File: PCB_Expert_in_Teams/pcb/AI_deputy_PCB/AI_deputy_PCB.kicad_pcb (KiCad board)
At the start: 2 copper layers, 15 parts, among them IC1 DA7280-00FVC, J1 Piezo Electric, U1 ESP32-WROOM-32UE_M113EH6400UH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, Y2 ABM8-40.000MHz-10-D1G-T

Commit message: progress on PCB + matlab calculations
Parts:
- removed U1: ESP32-WROOM-32UE_M113EH6400UH3Q0_, EXT_AI_DEPUTY_Library:MODULE_ESP32-WROOM-32UE_M113EH6400UH3Q0_
- removed Y2: ABM8-40.000MHz-10-D1G-T, EXT_AI_DEPUTY_Library:ABM810000MHZ12D2W
- added C10: 1u, Capacitor_SMD:C_0805_2012Metric_Pad1.18x1.45mm_HandSolder, F.Cu at (71.2, 62.7)
- added C11: 100n, Capacitor_SMD:C_0805_2012Metric_Pad1.18x1.45mm_HandSolder, F.Cu at (76.1, 53.6)
- added C12: 1u, Capacitor_SMD:C_0805_2012Metric_Pad1.18x1.45mm_HandSolder, F.Cu at (76.1, 56.6)
- added C13: 100n, Capacitor_SMD:C_0805_2012Metric_Pad1.18x1.45mm_HandSolder, F.Cu at (76.1, 59.6)
- added C14: 1u, Capacitor_SMD:C_0805_2012Metric_Pad1.18x1.45mm_HandSolder, F.Cu at (76.1, 62.7)
- added C15: 10u, Capacitor_SMD:C_0805_2012Metric_Pad1.18x1.45mm_HandSolder, F.Cu at (80.9, 53.6)
- added C16: 100n, Capacitor_SMD:C_0805_2012Metric_Pad1.18x1.45mm_HandSolder, F.Cu at (80.9, 56.6)
- added C17: 10u, Capacitor_SMD:C_0805_2012Metric_Pad1.18x1.45mm_HandSolder, F.Cu at (80.9, 59.6)
- added C18: 100n, Capacitor_SMD:C_0805_2012Metric_Pad1.18x1.45mm_HandSolder, F.Cu at (80.9, 62.7)
- added C19: 0.1u, Capacitor_SMD:C_0805_2012Metric_Pad1.18x1.45mm_HandSolder, F.Cu at (100.2, 71.5)
- added C20: 0.1u, Capacitor_SMD:C_0805_2012Metric_Pad1.18x1.45mm_HandSolder, F.Cu at (100.2, 74.5)
- added C21: 0.1u, Capacitor_SMD:C_0805_2012Metric_Pad1.18x1.45mm_HandSolder, F.Cu at (100.2, 77.5)
- added C22: 0.1u, Capacitor_SMD:C_0805_2012Metric_Pad1.18x1.45mm_HandSolder, F.Cu at (100.2, 80.6)
- added C23: 0.1u, Capacitor_SMD:C_0805_2012Metric_Pad1.18x1.45mm_HandSolder, F.Cu at (100.2, 83.6)
- added C24: 1u, Capacitor_SMD:C_0805_2012Metric_Pad1.18x1.45mm_HandSolder, F.Cu at (100.2, 86.6)
- added C25: 0.1u, Capacitor_SMD:C_0805_2012Metric_Pad1.18x1.45mm_HandSolder, F.Cu at (100.2, 89.6)
- added C26: 1u, Capacitor_SMD:C_0805_2012Metric_Pad1.18x1.45mm_HandSolder, F.Cu at (100.2, 92.6)
- added D1: LED, LED_SMD:LED_0805_2012Metric_Pad1.15x1.40mm_HandSolder, F.Cu at (86.5, 89.6)
- added IC2: DA7281-00FVC, EXT_AI_DEPUTY_Library:QFN65P300X300X84-12N, F.Cu at (66.2, 60.1)
- added IC3: DA7282-00FVC, EXT_AI_DEPUTY_Library:QFN65P300X300X84-12N, F.Cu at (66.2, 65.4)
- added IC4: IS31AP2005-SLS2-TR, EXT_AI_DEPUTY_Library:SOP65P490X110-8N, F.Cu at (131.3, 84.9)
- added IC5: IS31AP2005-SLS2-TR, EXT_AI_DEPUTY_Library:SOP65P490X110-8N, F.Cu at (131.3, 89.5)
- added IC6: LM25576QMH_NOPB, EXT_AI_DEPUTY_Library:SOP65P640X110-21N, F.Cu at (172.1, 74.1)
- added J10: OUTPUT Haptic B (Neck R), Connector_JST:JST_XH_S2B-XH-A_1x02_P2.50mm_Horizontal, F.Cu at (76.4, 41.9)
- added J11: OUTPUT Haptic C (Back), Connector_JST:JST_XH_S2B-XH-A_1x02_P2.50mm_Horizontal, F.Cu at (85.9, 41.9)
- added J12: Haptic Power and GND, Connector_JST:JST_XH_S2B-XH-A_1x02_P2.50mm_Horizontal, F.Cu at (95.3, 41.9)
- added J13: Conn_01x02_Socket, Connector_JST:JST_XH_S2B-XH-A-1_1x02_P2.50mm_Horizontal, F.Cu at (116.6, 73.9)
- added J14: Conn_01x02_Socket, Connector_JST:JST_XH_S2B-XH-A-1_1x02_P2.50mm_Horizontal, F.Cu at (126.1, 73.9)
- added J3: Haptic Power and GND, Connector_JST:JST_XH_S2B-XH-A_1x02_P2.50mm_Horizontal, F.Cu at (78.9, 94.6)
- added J4: UART, Connector_PinHeader_2.54mm:PinHeader_1x04_P2.54mm_Vertical, F.Cu at (87.2, 93.6)
- added J5: JST CONN from MCU, Connector_JST:JST_XH_S3B-XH-A_1x03_P2.50mm_Horizontal, F.Cu at (67.0, 94.6)
- added J6: JTAG, Connector_PinHeader_2.54mm:PinHeader_1x04_P2.54mm_Vertical, F.Cu at (91.8, 93.6)
- added J7: JST CONN from MCU, Connector_JST:JST_XH_S3B-XH-A_1x03_P2.50mm_Horizontal, F.Cu at (86.8, 55.5)
- added J8: Conn_01x04_Socket, Connector_JST:JST_XH_S4B-XH-A-1_1x04_P2.50mm_Horizontal, F.Cu at (116.6, 87.5)
- added J9: OUTPUT Haptic A (Neck L), Connector_JST:JST_XH_S2B-XH-A_1x02_P2.50mm_Horizontal, F.Cu at (67.0, 41.9)
- added Q1: NMOS, Package_TO_SOT_SMD:TO-252-3_TabPin2, F.Cu at (113.7, 46.5)
- added R10: 150k, Resistor_SMD:R_0805_2012Metric_Pad1.20x1.40mm_HandSolder, F.Cu at (105.0, 74.5)
- added R11: 150k, Resistor_SMD:R_0805_2012Metric_Pad1.20x1.40mm_HandSolder, F.Cu at (105.0, 77.4)
- added R12: 150k, Resistor_SMD:R_0805_2012Metric_Pad1.20x1.40mm_HandSolder, F.Cu at (105.0, 80.3)
- added R13: 100k, Resistor_SMD:R_0805_2012Metric_Pad1.20x1.40mm_HandSolder, F.Cu at (105.0, 83.3)
- added R14: 100k, Resistor_SMD:R_0805_2012Metric_Pad1.20x1.40mm_HandSolder, F.Cu at (105.0, 86.2)
- added R5: 4.7k, Resistor_SMD:R_0805_2012Metric_Pad1.20x1.40mm_HandSolder, F.Cu at (97.6, 56.5)
- added R6: 4.7k, Resistor_SMD:R_0805_2012Metric_Pad1.20x1.40mm_HandSolder, F.Cu at (97.6, 59.5)
- added R7: 10k, Resistor_SMD:R_0805_2012Metric_Pad1.20x1.40mm_HandSolder, F.Cu at (91.2, 84.1)
- added R8: 10k, Resistor_SMD:R_0805_2012Metric_Pad1.20x1.40mm_HandSolder, F.Cu at (91.2, 87.0)
- added R9: 150k, Resistor_SMD:R_0805_2012Metric_Pad1.20x1.40mm_HandSolder, F.Cu at (105.0, 71.5)
- added U2: ESP32-WROOM-32UE, RF_Module:ESP32-WROOM-32UE, F.Cu at (134.3, 54.5)
- C2: value C -> 10u
- C4, C5: value 27pF -> 100n
- C6: value C -> 10uF
- C7: value C -> 1uF
- C8, C9: value C -> 0.1uF
- R1: value R -> 4.7k
- moved J1 53.1 mm to (111.5, 63.1)
- moved C1 29.1 mm to (86.5, 71.5)
- moved C3 26.5 mm to (86.5, 74.5)
- moved C7 21.8 mm to (86.5, 80.6)
- moved C6 21.8 mm to (86.5, 77.5)
- moved C8 21.8 mm to (86.5, 83.6)
- moved C9 21.8 mm to (86.5, 86.6)
- moved IC1 16.9 mm to (66.2, 54.8)
- moved R1 16.0 mm to (97.6, 53.6)
- moved R3 10.5 mm to (91.2, 81.1)
- moved C2 4.10 mm to (71.2, 53.6)
- moved C4 1.14 mm to (71.2, 56.6)
- moved C5 1.14 mm to (71.2, 59.6)
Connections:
- C2 pad 1: unconnected-(C2-Pad1) -> +3V3
- C2 pad 2: unconnected-(C2-Pad2) -> GND
- C4 pad 1: GND -> +3V3
- C4 pad 2: Net-(Y2-GND_1) -> GND
- C5 pad 1: Net-(Y2-GND_2) -> +3V3
- C9 pad 2: GND -> VDD
- IC1 pad 1: unconnected-(IC1-GPI_2-Pad1) -> GND
- IC1 pad 10: unconnected-(IC1-SDA-Pad10) -> SDA
- IC1 pad 11: unconnected-(IC1-SCL-Pad11) -> SCL
- IC1 pad 12: unconnected-(IC1-NIRQ-Pad12) -> NIRQ
- IC1 pad 2: unconnected-(IC1-GPI_1-Pad2) -> GND
- IC1 pad 3: unconnected-(IC1-GPI_0/_PWM-Pad3) -> GND
- IC1 pad 4: unconnected-(IC1-VDD-Pad4) -> +3V3
- IC1 pad 5: unconnected-(IC1-OUTP-Pad5) -> Net-(IC1-OUTP)
- IC1 pad 6: unconnected-(IC1-GND_1-Pad6) -> GND
- IC1 pad 7: unconnected-(IC1-GND_2-Pad7) -> GND
- IC1 pad 8: unconnected-(IC1-OUTN-Pad8) -> Net-(IC1-OUTN)
- IC1 pad 9: unconnected-(IC1-VDDIO-Pad9) -> +3V3
- R1 pad 1: unconnected-(R1-Pad1) -> +3V3
- R1 pad 2: unconnected-(R1-Pad2) -> NIRQ

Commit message: 29/10/update
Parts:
- added C28: 0.01u, Capacitor_SMD:C_0805_2012Metric_Pad1.18x1.45mm_HandSolder, F.Cu at (144.8, 90.3)
- added C29: 82p, Capacitor_SMD:C_0805_2012Metric_Pad1.18x1.45mm_HandSolder, F.Cu at (144.8, 93.3)
- added C30: 0.01u, Capacitor_SMD:C_0805_2012Metric_Pad1.18x1.45mm_HandSolder, F.Cu at (144.8, 96.3)
- added C31: 0.1u, Capacitor_SMD:C_0805_2012Metric_Pad1.18x1.45mm_HandSolder, F.Cu at (144.8, 99.3)
- added C32: 22nF, Capacitor_SMD:C_0805_2012Metric_Pad1.18x1.45mm_HandSolder, F.Cu at (144.8, 102.3)
- added C34: 10u, Capacitor_SMD:C_0805_2012Metric_Pad1.18x1.45mm_HandSolder, F.Cu at (144.8, 105.3)
- added C35: 10u, Capacitor_SMD:C_0805_2012Metric_Pad1.18x1.45mm_HandSolder, F.Cu at (144.8, 108.3)
- added C36: 10u, Capacitor_SMD:C_0805_2012Metric_Pad1.18x1.45mm_HandSolder, F.Cu at (144.8, 111.3)
- added C37: 10u, Capacitor_SMD:C_0805_2012Metric_Pad1.18x1.45mm_HandSolder, F.Cu at (144.8, 114.3)
- added D2: MBRS540T3G, EXT_AI_DEPUTY_Library:DIOM7958X256N, F.Cu at (152.6, 107.3)
- added D3: LED, LED_SMD:LED_0805_2012Metric_Pad1.15x1.40mm_HandSolder, F.Cu at (171.9, 101.3)
- added J16: USB_C_Receptacle_USB2.0_16P, EXT_AI_DEPUTY_Library:MOLEX_1054500101, F.Cu at (175.2, 98.8)
- added R15: 49.9k, Resistor_SMD:R_0805_2012Metric_Pad1.20x1.40mm_HandSolder, F.Cu at (149.6, 90.2)
- added R16: 10k, Resistor_SMD:R_0805_2012Metric_Pad1.20x1.40mm_HandSolder, F.Cu at (149.6, 93.2)
- added R17: 5.11k, Resistor_SMD:R_0805_2012Metric_Pad1.20x1.40mm_HandSolder, F.Cu at (149.6, 96.1)
- added R18: 3.01k, Resistor_SMD:R_0805_2012Metric_Pad1.20x1.40mm_HandSolder, F.Cu at (149.6, 99.1)
- added R19: 510, Resistor_SMD:R_0805_2012Metric_Pad1.20x1.40mm_HandSolder, F.Cu at (149.6, 102.0)
- added R20: 5.1k, Resistor_SMD:R_0805_2012Metric_Pad1.20x1.40mm_HandSolder, F.Cu at (162.4, 90.2)
- added R21: 1k, Resistor_SMD:R_0805_2012Metric_Pad1.20x1.40mm_HandSolder, F.Cu at (162.4, 93.2)
- added R22: 5.1k, Resistor_SMD:R_0805_2012Metric_Pad1.20x1.40mm_HandSolder, F.Cu at (162.4, 96.1)
- added R23: 2.4k, Resistor_SMD:R_0805_2012Metric_Pad1.20x1.40mm_HandSolder, F.Cu at (162.4, 99.1)
- added R24: 5.1k, Resistor_SMD:R_0805_2012Metric_Pad1.20x1.40mm_HandSolder, F.Cu at (162.4, 102.0)
- added R25: 1k, Resistor_SMD:R_0805_2012Metric_Pad1.20x1.40mm_HandSolder, F.Cu at (162.4, 105.0)
- added R26: 2.2k, Resistor_SMD:R_0805_2012Metric_Pad1.20x1.40mm_HandSolder, F.Cu at (167.1, 90.2)
- added R33: 10k, Resistor_SMD:R_0805_2012Metric_Pad1.20x1.40mm_HandSolder, F.Cu at (167.1, 93.2)
- added R34: 4.7k, Resistor_SMD:R_0805_2012Metric_Pad1.20x1.40mm_HandSolder, F.Cu at (167.1, 96.1)
- added R35: 1k, Resistor_SMD:R_0805_2012Metric_Pad1.20x1.40mm_HandSolder, F.Cu at (167.1, 99.1)
- added R36: 50k, Resistor_SMD:R_0805_2012Metric_Pad1.20x1.40mm_HandSolder, F.Cu at (167.1, 102.0)
- J1: footprint Connector_JST:JST_XH_B1B-XH-AM_1x01_P2.50mm_Vertical -> Connector_JST:JST_XH_S2B-XH-A-1_1x02_P2.50mm_Horizontal
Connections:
- IC6 pad 1: unconnected-(IC6-VCC-Pad1) -> Net-(IC6-VCC)
- IC6 pad 10: unconnected-(IC6-AGND-Pad10) -> GND
- IC6 pad 11: unconnected-(IC6-SS-Pad11) -> Net-(IC6-SS)
- IC6 pad 12: unconnected-(IC6-OUT-Pad12) -> +3V3
- IC6 pad 13: unconnected-(IC6-PGND_1-Pad13) -> GND
- IC6 pad 14: unconnected-(IC6-PGND_2-Pad14) -> GND
- IC6 pad 15: unconnected-(IC6-IS_1-Pad15) -> Net-(D2-A)
- IC6 pad 16: unconnected-(IC6-IS_2-Pad16) -> Net-(D2-A)
- IC6 pad 17: unconnected-(IC6-SW_1-Pad17) -> Net-(D2-K)
- IC6 pad 18: unconnected-(IC6-SW_2-Pad18) -> Net-(D2-K)
- IC6 pad 19: unconnected-(IC6-PRE-Pad19) -> Net-(D2-K)
- IC6 pad 20: unconnected-(IC6-BST-Pad20) -> Net-(IC6-BST)
- IC6 pad 21: unconnected-(IC6-EP-Pad21) -> GND
- IC6 pad 3: unconnected-(IC6-VIN_1-Pad3) -> VIN
- IC6 pad 4: unconnected-(IC6-VIN_2-Pad4) -> VIN
- IC6 pad 5: unconnected-(IC6-SYNC-Pad5) -> GND
- IC6 pad 6: unconnected-(IC6-COMP-Pad6) -> Net-(IC6-COMP)
- IC6 pad 7: unconnected-(IC6-FB-Pad7) -> Net-(IC6-FB)
- IC6 pad 8: unconnected-(IC6-RT-Pad8) -> Net-(IC6-RT)
- IC6 pad 9: unconnected-(IC6-RAMP-Pad9) -> Net-(IC6-RAMP)
- U2 pad 10: unconnected-(U2-IO25-Pad10) -> Signal Left
- U2 pad 11: unconnected-(U2-IO26-Pad11) -> Signal Right

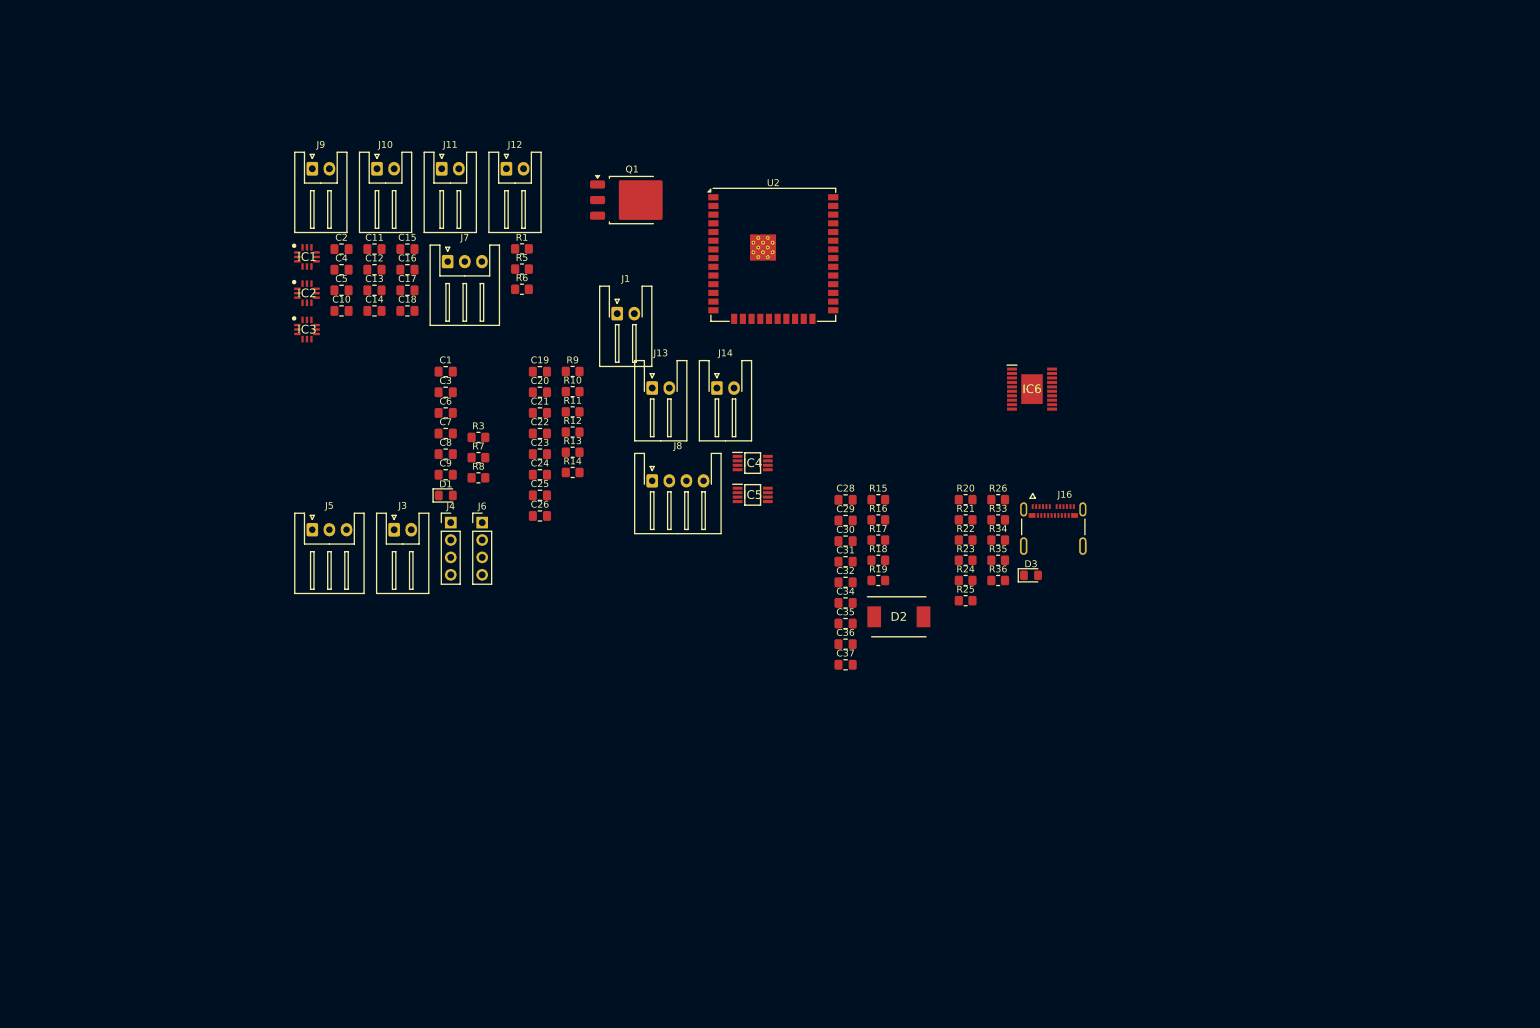
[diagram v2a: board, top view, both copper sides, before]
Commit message: update some schematic footprints
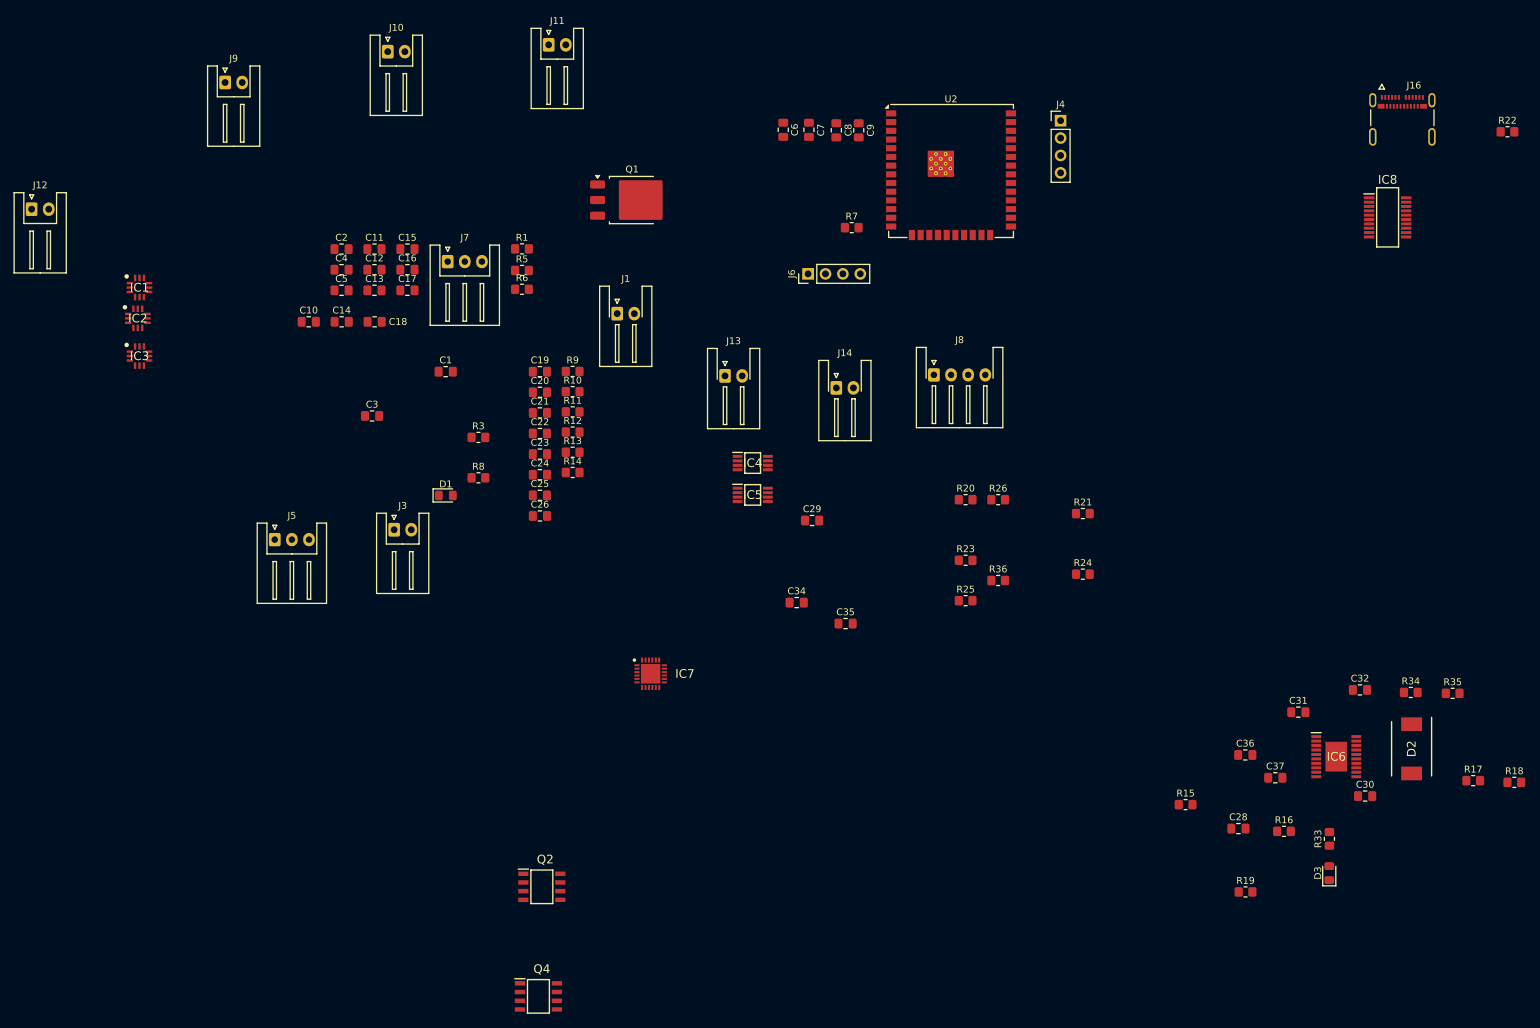
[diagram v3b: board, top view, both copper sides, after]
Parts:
- added IC7: CYPD3177-24LQXQ, EXT_AI_DEPUTY_Library:QFN50P400X400X60-25N-D, F.Cu at (116.4, 115.6)
- added IC8: FT231XS-R, EXT_AI_DEPUTY_Library:SOP64P599X175-20N, F.Cu at (224.0, 49.0)
- added Q2: DMP3098LSD-13, EXT_AI_DEPUTY_Library:SOIC127P600X175-8N, F.Cu at (100.5, 146.8)
- added Q4: DMP3098LSD-13, EXT_AI_DEPUTY_Library:SOIC127P600X175-8N, F.Cu at (100.0, 162.8)
- moved J4 106.7 mm to (176.2, 34.9)
- moved R22 99.1 mm to (241.5, 36.5)
- moved R18 98.4 mm to (242.5, 131.5)
- moved R17 93.7 mm to (236.5, 131.2)
- moved C30 84.5 mm to (220.7, 133.5)
- moved J16 78.5 mm to (226.2, 39.0)
- moved C9 78.5 mm to (146.8, 36.3), turned to 90 degrees
- moved D2 77.3 mm to (227.5, 126.6), turned to -90 degrees
- moved C32 76.7 mm to (220.0, 118.0)
- moved C28 74.8 mm to (202.2, 138.2)
- moved R16 74.7 mm to (208.9, 138.7)
- moved C8 74.1 mm to (143.5, 36.3), turned to -90 degrees
- moved R19 70.3 mm to (203.2, 147.5)
- moved IC6 69.7 mm to (216.5, 127.8)
- moved C31 69.7 mm to (211.0, 121.2)
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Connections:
- net Net-(J4-Pin_2) renamed USB_RX
- net Net-(J4-Pin_3) renamed USB_TX
- C9 pad 1: Net-(C9-Pad1) -> GND
- C9 pad 2: VDD -> +3V3
- U2 pad 2: VDD33 -> +3V3

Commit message: update pcb from desktop
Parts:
- removed J16: USB_C_Receptacle_USB2.0_16P, EXT_AI_DEPUTY_Library:MOLEX_1054500101
- added C27: 68u, EXT_AI_DEPUTY_Library:T520D, F.Cu at (199.0, 125.6)
- added C33: 150u, EXT_AI_DEPUTY_Library:SX_Package, F.Cu at (236.0, 127.8)
- added C38: 4u7, Capacitor_SMD:C_0805_2012Metric_Pad1.18x1.45mm_HandSolder, F.Cu at (216.1, 51.9)
- added C39: 100n, Capacitor_SMD:C_0805_2012Metric_Pad1.18x1.45mm_HandSolder, F.Cu at (220.1, 52.0)
- added C40: 100n, Capacitor_SMD:C_0805_2012Metric_Pad1.18x1.45mm_HandSolder, F.Cu at (224.8, 52.0)
- added C41: 4u7, Capacitor_SMD:C_0805_2012Metric_Pad1.18x1.45mm_HandSolder, F.Cu at (231.6, 42.3)
- added C42: 100n, Capacitor_SMD:C_0805_2012Metric_Pad1.18x1.45mm_HandSolder, F.Cu at (226.3, 42.2)
- added C45: 4u7, Capacitor_SMD:C_0805_2012Metric_Pad1.18x1.45mm_HandSolder, F.Cu at (211.7, 84.0)
- added C48: 4u7, Capacitor_SMD:C_0805_2012Metric_Pad1.18x1.45mm_HandSolder, F.Cu at (211.7, 87.0)
- added C49: 100n, Capacitor_SMD:C_0805_2012Metric_Pad1.18x1.45mm_HandSolder, F.Cu at (211.7, 90.0)
- added L2: 8.2u, EXT_AI_DEPUTY_Library:INDPM7166X300N, F.Cu at (237.8, 118.5)
- added R2: 10k, Resistor_SMD:R_0805_2012Metric_Pad1.20x1.40mm_HandSolder, F.Cu at (237.8, 77.2)
- added R27: 2k2, Resistor_SMD:R_0805_2012Metric_Pad1.20x1.40mm_HandSolder, F.Cu at (254.1, 46.8)
- added R28: 2k2, Resistor_SMD:R_0805_2012Metric_Pad1.20x1.40mm_HandSolder, F.Cu at (254.1, 49.7)
- added R29: 2k2, Resistor_SMD:R_0805_2012Metric_Pad1.20x1.40mm_HandSolder, F.Cu at (256.2, 55.0)
- added R30: 20k, Resistor_SMD:R_0805_2012Metric_Pad1.20x1.40mm_HandSolder, F.Cu at (231.0, 86.1)
- added R31: 2k2, Resistor_SMD:R_0805_2012Metric_Pad1.20x1.40mm_HandSolder, F.Cu at (231.0, 89.0)
- added R32: 2k2, Resistor_SMD:R_0805_2012Metric_Pad1.20x1.40mm_HandSolder, F.Cu at (231.0, 92.0)
- added R4: 10k, Resistor_SMD:R_0805_2012Metric_Pad1.20x1.40mm_HandSolder, F.Cu at (237.8, 80.2)
- moved Q2 182.8 mm to (263.8, 64.6)
- moved Q4 177.8 mm to (249.8, 66.9)
- moved IC7 133.0 mm to (231.8, 49.5), turned to 90 degrees
- moved J5 128.8 mm to (185.0, 59.6)
- moved J3 122.9 mm to (187.8, 37.5), turned to 90 degrees
- moved C34 106.8 mm to (242.5, 126.0), turned to -90 degrees
- moved C35 104.7 mm to (248.0, 126.0), turned to -90 degrees
- moved D3 100.0 mm to (246.4, 49.6), turned to 180 degrees
- moved R35 94.9 mm to (138.6, 119.1)
- moved R33 94.1 mm to (242.6, 49.6), turned to 0 degrees
- moved R23 83.6 mm to (236.7, 60.7), turned to -90 degrees
- moved C29 82.4 mm to (214.0, 129.5), turned to -90 degrees
- moved R25 79.3 mm to (228.3, 60.9), turned to -90 degrees
- moved R26 78.1 mm to (239.4, 60.6), turned to -90 degrees
- moved J11 75.3 mm to (55.3, 83.2), turned to 90 degrees
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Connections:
- Q4 pad 5: unconnected-(Q4-D2_1-Pad5) -> VDC_OUT
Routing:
- net +3V3: track 0.12 -> 276.3 mm
- net NIRQ: track 0.00 -> 71.4 mm, vias 0 -> 7
- net SCL: track 0.00 -> 68.1 mm, vias 0 -> 4
- net Net-(IC6-FB): track 0.00 -> 64.7 mm
- net SDA: track 0.00 -> 58.1 mm, vias 0 -> 5
- net Net-(D2-A): track 0.00 -> 23.6 mm
- net TDO: track 0.00 -> 20.6 mm
- net VIN: track 0.00 -> 19.3 mm
- net Net-(D2-K): track 0.00 -> 19.0 mm
- net Net-(IC1-OUTP): track 0.00 -> 16.1 mm, vias 0 -> 2
- net TMS: track 0.00 -> 15.5 mm
- net Net-(IC7-VBUS_MIN): track 0.00 -> 14.6 mm
- net TCK: track 0.00 -> 14.3 mm
- net VBUS: track 0.00 -> 13.3 mm
- net Net-(IC7-VBUS_MAX): track 0.00 -> 13.1 mm
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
